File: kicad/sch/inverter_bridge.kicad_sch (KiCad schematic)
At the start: 12 parts, among them J4 MOTOR U/V/W/PE, Q10 C3M0075120K, Q11 C3M0075120K, Q12 C3M0075120K, Q7 C3M0075120K, Q8 C3M0075120K, Q9 C3M0075120K

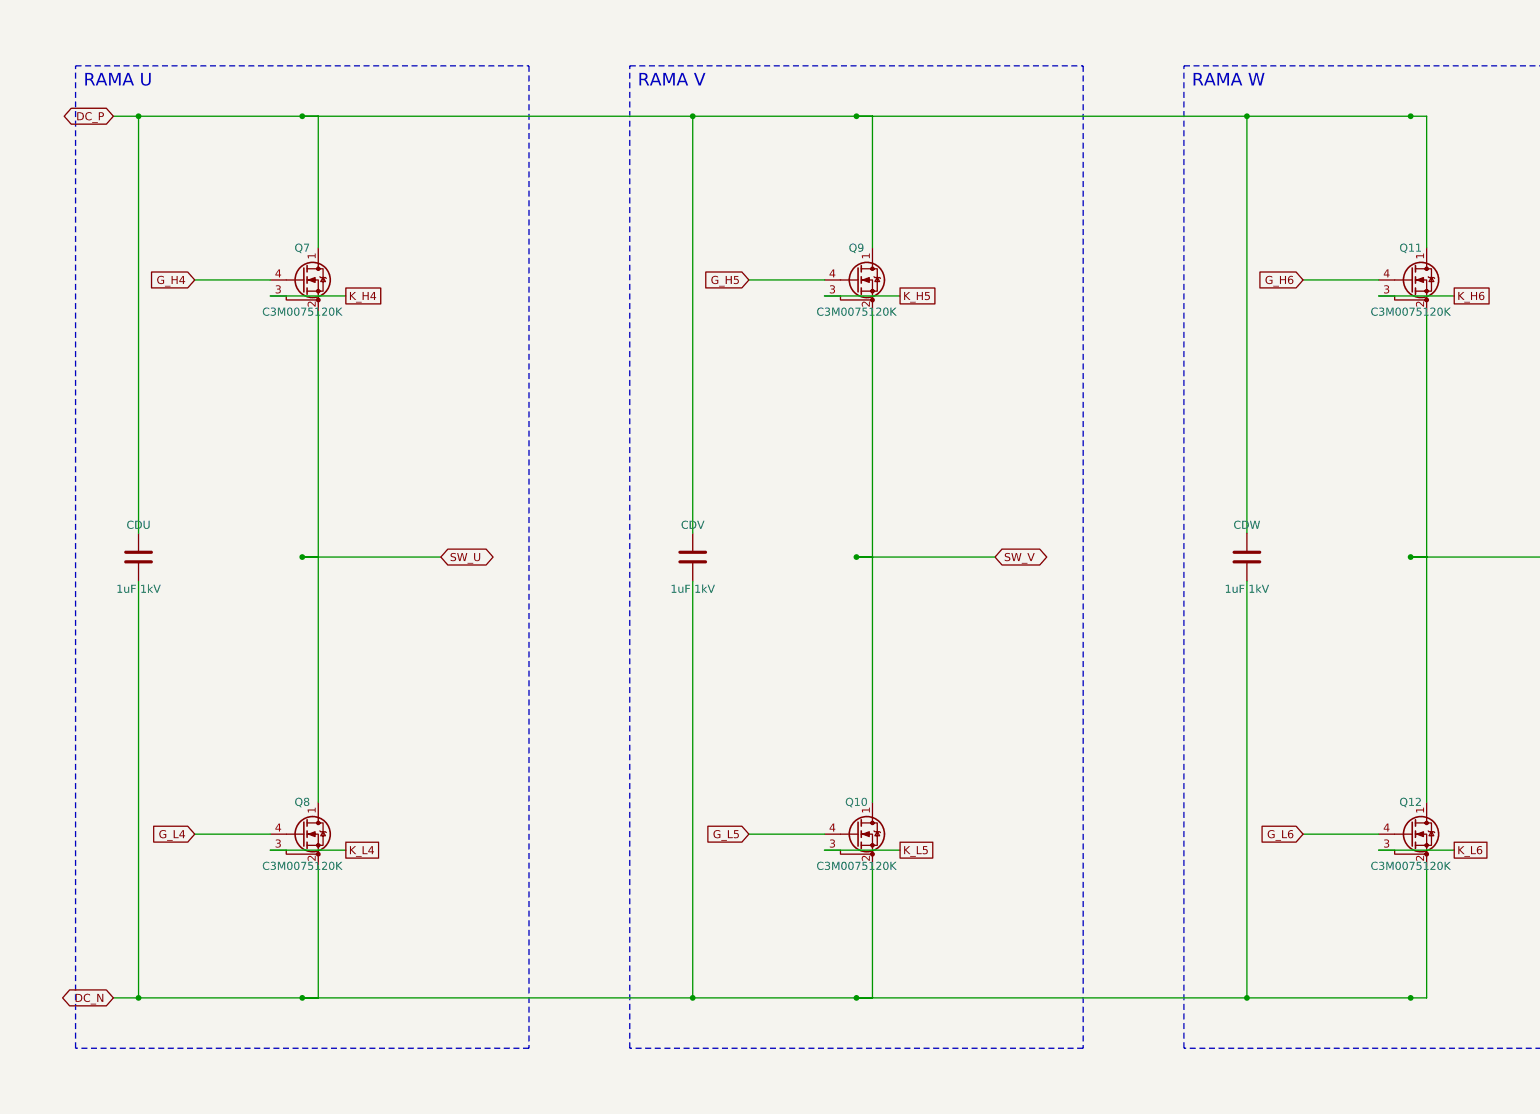
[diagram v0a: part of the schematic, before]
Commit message: Corrige tres bugs de conectividad del bus DC y anade guia de simulacion
Al intentar rutear los lazos de conmutacion aparecieron tres errores graves
del esquematico que ninguna revision visual habia detectado:

1. Los rieles del bus DC solo conectaban la ULTIMA rama de cada puente.
   DC_P tenia 4 pads en vez de 22; Q1, Q3, Q7 y Q9 quedaban unconnected.
   Causa: el riel era un unico cable largo y los stubs de cada rama morian
   en mitad de el. KiCad solo une cables extremo con extremo: un cable que
   termina en medio de otro NO conecta, ni con junction. Solo funcionaba la
   ultima rama porque coincidia con el extremo del riel.
   Corregido con un helper rail() que construye el riel PARTIDO en cada
   punto de contacto.

2. El puente AFE no estaba conectado al filtro LCL: el nodo de conmutacion
   se llamaba SW_A y la salida del LCL AFE_A. Mismo nodo fisico, dos
   nombres. Unificado a AFE_A/B/C.

3. La resistencia de precarga quedaba puenteada porque el helper de riel
   se tragaba tambien el nodo DC_RAW. Corregido acotando con xmin.

Resultado: DC_P de 4 a 22 pads, DC_N de 4 a 18.

Tambien: se probo extender el bus laminado sobre toda la fila de potencia y
EMPEORA (293 clearance, 34 cortos): con 3 mm exigidos a HV_DC y los pines
del TO-247-4 a 2.54 mm el plano no cabe entre drenador y puerta. Revertido y
documentado.

Nuevo: docs/COMO_SIMULAR.md con las cuatro simulaciones del proyecto.

Co-Authored-By: Claude Opus 5 <noreply@anthropic.com>
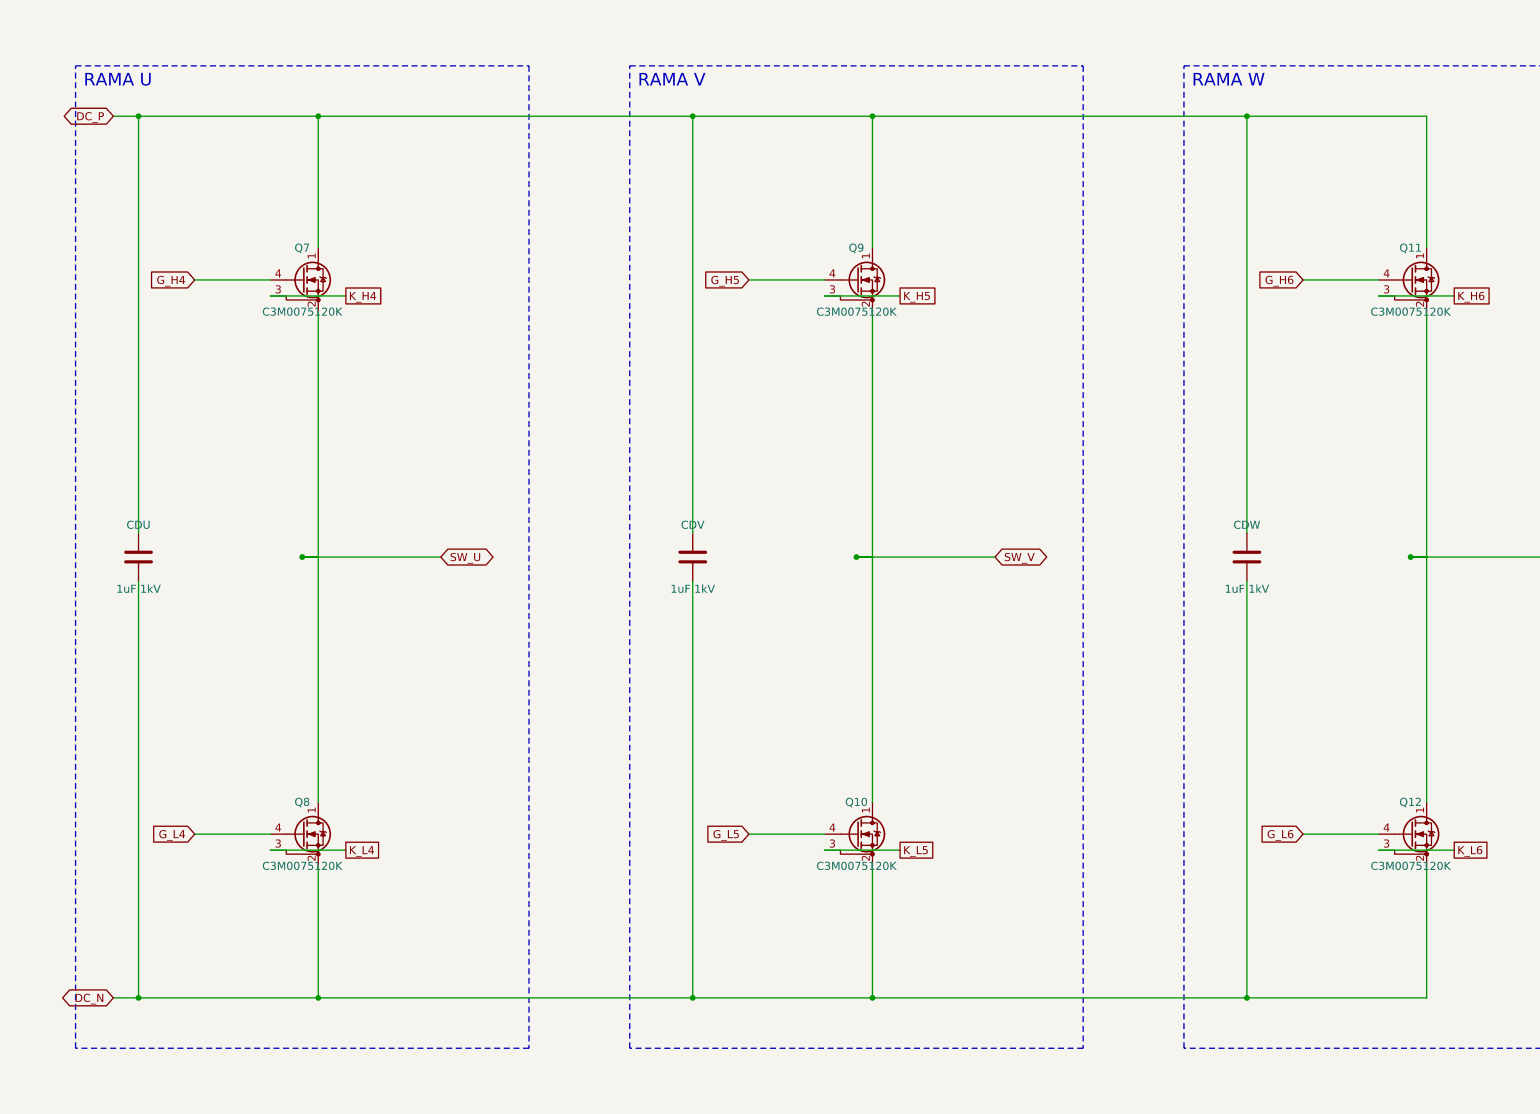
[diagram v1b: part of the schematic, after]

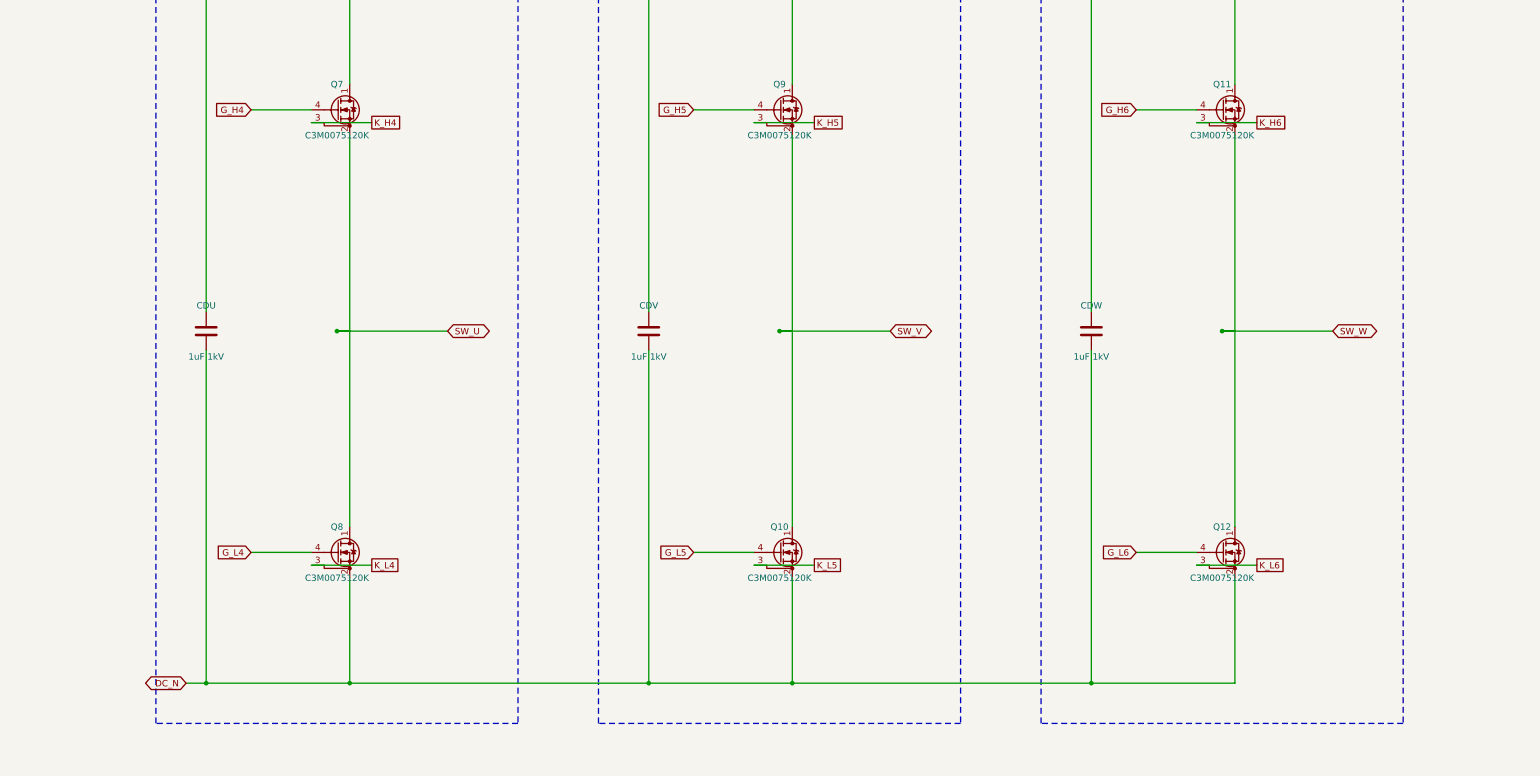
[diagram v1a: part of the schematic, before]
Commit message: Anade protecciones electricas y stackup con color
PROTECCIONES (de 15 a 56 componentes de proteccion, 272 en total)

  12x TVS gate-source, una por SiC. Sin ella un pico de dv/dt acoplado
      por Cgd puede perforar el oxido de puerta: es el modo de fallo mas
      comun en SiC. Va en el pie del transistor.
  12x snubber RC del nodo de conmutacion (220 pF + 4.7 ohm). El valor sale
      del barrido en LTspice: baja el dv/dt de 147 a 90 V/ns, por debajo
      del CMTI de 100 V/ns del UCC21520, y la sobretension de 823 a 767 V.
   2x TVS en serie sobre el bus DC (5KP440A): recorte en nanosegundos muy
      por delante del chopper, que es un lazo de control.
  12x Schottky de recorte en las entradas de ADC. La R serie del filtro
      anti-alias limita la corriente; sin los diodos, un transitorio de la
      etapa de potencia entra directo al pin del STM32.
   4x TVS de ESD en el conector de campo del ESP32.
   1x polyfuse rearmable + diodo antiinversion + TVS en la entrada de 24 V.

BUGS DESTAPADOS AL CABLEAR LAS PROTECCIONES

  a) Los 4 TVS del conector de campo compartian columna: sus bajadas a
     IOGND se solapaban y cortocircuitaban las cuatro lineas. Cada uno a
     su propia x.
  b) Los diodos de recorte del ADC morian en MITAD del cable de senal, asi
     que KiCad no los conectaba (solo une extremo con extremo, el mismo
     fallo que ya aparecio en los rieles del bus). El cable se parte ahora
     en el punto de recorte.

ASPECTO

  El .kicad_pcb no tenia seccion (stackup), por eso el render salia verde
  por defecto. Se inyecta desde tools/stackup_tpl.txt: mascara negra,
  serigrafia blanca, acabado ENIG (obligado con el LQFP-100 de paso
  0.5 mm) y los espesores reales de cobre (70 um exteriores, 35 um
  interiores) con prepreg fino de 0.2 mm entre F.Cu e In1.Cu para que el
  bus laminado tenga poca inductancia. Los colores son parametros al
  principio de tools/gen_pcb.py.

Co-Authored-By: Claude Opus 5 <noreply@anthropic.com>
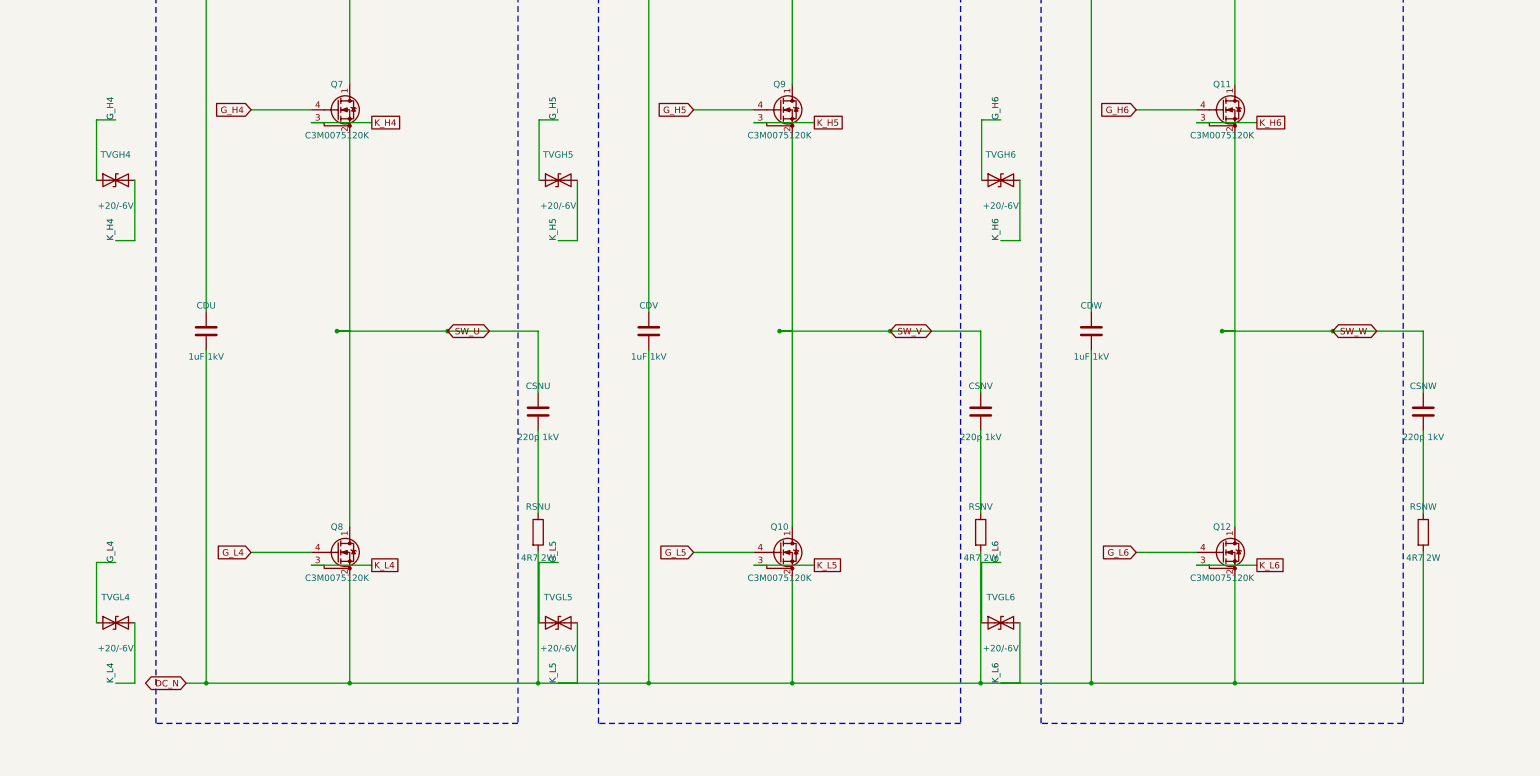
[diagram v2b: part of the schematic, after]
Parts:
- added CSNU, CSNV, CSNW: 220p 1kV, Capacitor_THT:C_Rect_L24.0mm_W10.3mm_P22.50mm_MKT, symbol Device:C
- added RSNU, RSNV, RSNW: 4R7 2W, Resistor_SMD:R_2512_6332Metric, symbol Device:R
- added TVGH4, TVGH5, TVGH6, TVGL4, TVGL5, TVGL6: +20/-6V, Diode_SMD:D_SOD-123, symbol Device:D_TVS
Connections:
- net K_L5 is gone; now on net DC_N: Q10.3 (DS)
- net K_L6 is gone; now on net DC_N: Q12.3 (DS)
- net DC_N: now also RSNU.2, RSNV.2, RSNW.2, TVGL5.2 (A2), TVGL6.2 (A2)
- net G_H4: now also TVGH4.1 (A1)
- net G_H5: now also TVGH5.1 (A1)
- net G_H6: now also TVGH6.1 (A1)
- net G_L4: now also TVGL4.1 (A1)
- net G_L5: now also TVGL5.1 (A1)
- net G_L6: now also TVGL6.1 (A1)
- net K_H4: now also TVGH4.2 (A2)
- net K_H5: now also TVGH5.2 (A2)
- net K_H6: now also TVGH6.2 (A2)
- net K_L4: now also TVGL4.2 (A2)
- net SW_U: now also CSNU.1
- net SW_V: now also CSNV.1
- net SW_W: now also CSNW.1
- new net: CSNU.2, RSNU.1
- new net: CSNV.2, RSNV.1
- new net: CSNW.2, RSNW.1
